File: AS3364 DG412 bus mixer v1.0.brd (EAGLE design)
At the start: 88.9 x 49.2 mm, 118 parts, among them IC1 PCA9539PW, IC10 DG412-J, IC11 DG412-J, IC14 TL074JT, IC2 TL074JT, IC3 TL072JT, IC4 TL074JT, IC6 TL072JT, IC8 DG412-J, IC9 DG412-J

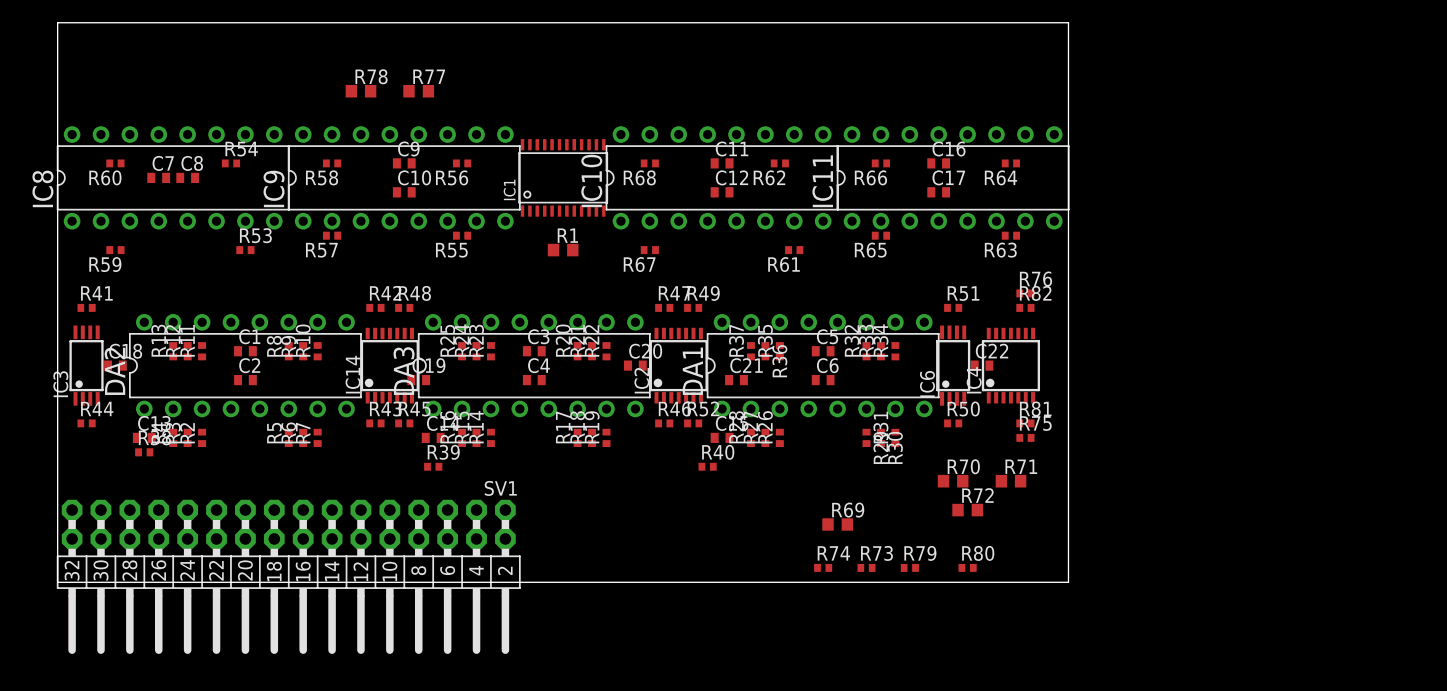
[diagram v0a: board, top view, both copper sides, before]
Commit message: Finished tracing switches and vcas internally
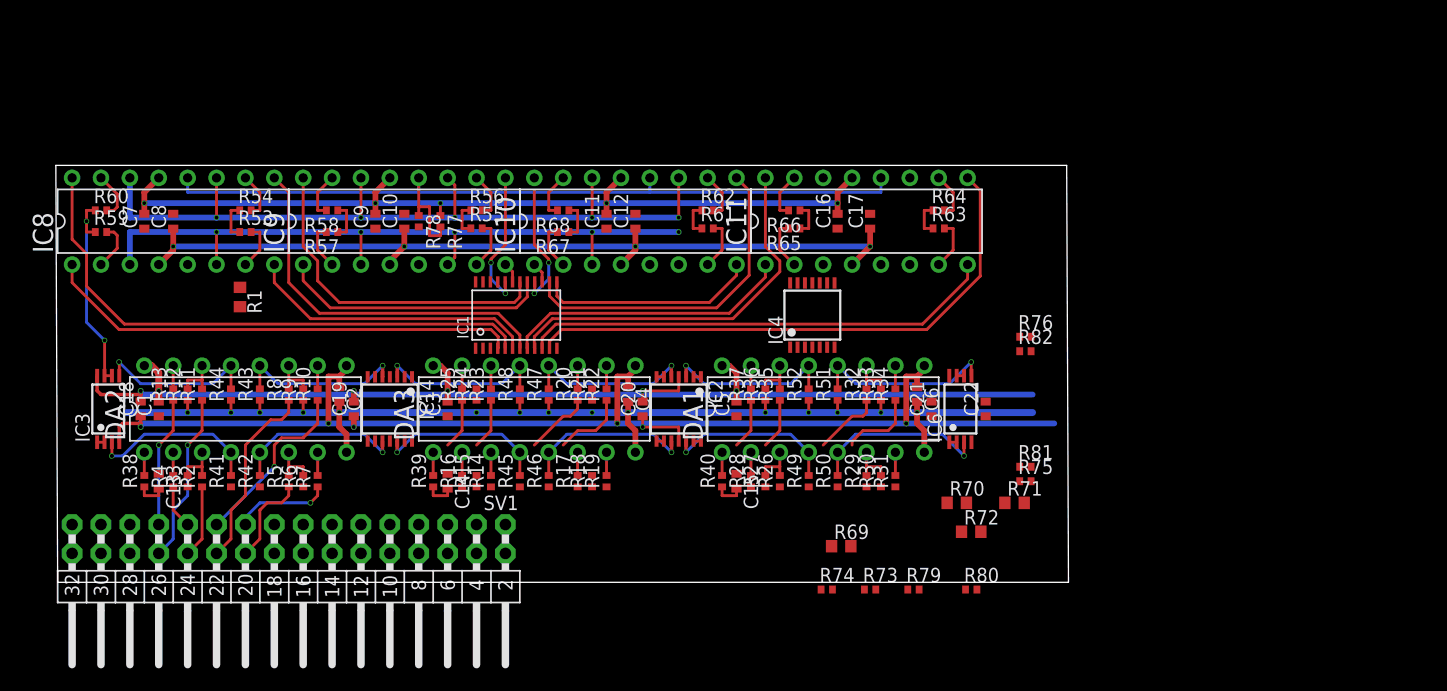
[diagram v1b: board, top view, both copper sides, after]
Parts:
- R77, R78: device rcl:R0603 -> rcl:R0402
- moved R1 28.7 mm to (16.0, 25.1), turned to 270 degrees
- moved R41 19.8 mm to (15.2, 8.89), turned to 90 degrees
- moved R49 18.3 mm to (66.0, 8.89), turned to 90 degrees
- moved R42 18.3 mm to (17.8, 8.89), turned to 90 degrees
- moved IC4 18.0 mm to (66.4, 23.5)
- moved C21 17.3 mm to (76.8, 15.2), turned to 90 degrees
- moved R44 13.0 mm to (15.2, 16.5), turned to 90 degrees
- moved IC1 12.8 mm to (40.3, 23.5)
- moved R47 12.7 mm to (43.2, 16.5), turned to 90 degrees
- moved R48 12.7 mm to (40.6, 16.5), turned to 90 degrees
- moved R51 12.7 mm to (68.6, 16.5), turned to 90 degrees
- moved R78 12.5 mm to (31.8, 31.8), turned to 270 degrees
- moved R77 11.6 mm to (33.7, 31.8), turned to 270 degrees
- moved C11 11.4 mm to (48.3, 31.8), turned to 90 degrees
- moved R46 11.4 mm to (43.2, 8.89), turned to 90 degrees
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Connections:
- net CON1: now also IC3.5; no longer IC3.3
- net CON2: now also IC3.3; no longer IC3.5
- net CON3: now also IC14.5; no longer IC14.3
- net CON4: now also IC14.10; no longer IC14.12
- net CON5: now also IC14.3; no longer IC14.5
- net CON6: now also IC14.12; no longer IC14.10
- net CON7: now also IC2.5; no longer IC2.3
- net CON8: now also IC2.10; no longer IC2.12
- net CON_O1: now also IC2.3; no longer IC2.5
- net CON_O2: now also IC2.12; no longer IC2.10
- net CON_O3: now also IC6.5; no longer IC6.3
- net CON_O4: now also IC6.3; no longer IC6.5
- net DIG_3_BUS_A: now also IC1.17; no longer IC1.8
- net DIG_3_BUS_B: now also IC1.18; no longer IC1.9
- net DIG_4_BUS_A: now also IC1.19; no longer IC1.10
- net DIG_4_BUS_B: now also IC1.20; no longer IC1.11
- net DIG_5_BUS_A: now also IC1.15; no longer IC1.13
- net DIG_5_BUS_B: now also IC1.16; no longer IC1.14
- net DIG_6_BUS_A: now also IC1.13; no longer IC1.15
- net DIG_6_BUS_B: now also IC1.14; no longer IC1.16
- net DIG_7_BUS_A: now also IC1.8; no longer IC1.17
- net DIG_7_BUS_B: now also IC1.9; no longer IC1.18
- net DIG_8_BUS_A: now also IC1.10; no longer IC1.19
- net DIG_8_BUS_B: now also IC1.11; no longer IC1.20
- net OUT1: now also IC3.6, IC3.7; no longer IC3.1, IC3.2
- net OUT2: now also IC3.1, IC3.2; no longer IC3.6, IC3.7
- net OUT3: now also IC14.6, IC14.7; no longer IC14.1, IC14.2
- net OUT4: now also IC14.8, IC14.9; no longer IC14.13, IC14.14
- net OUT5: now also IC14.1, IC14.2; no longer IC14.6, IC14.7
- net OUT6: now also IC14.13, IC14.14; no longer IC14.8, IC14.9
- net OUT7: now also IC2.6, IC2.7; no longer IC2.1, IC2.2
- net OUT8: now also IC2.8, IC2.9; no longer IC2.13, IC2.14
- net OUT_A: now also IC2.1, IC2.2; no longer IC2.6, IC2.7
- net OUT_B: now also IC2.13, IC2.14; no longer IC2.8, IC2.9
- net OUT_FX_A: now also IC6.6, IC6.7; no longer IC6.1, IC6.2
- net OUT_FX_B: now also IC6.1, IC6.2; no longer IC6.6, IC6.7
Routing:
- net -12V: track 0.00 -> 189.7 mm, vias 0 -> 10
- net +12V: track 0.00 -> 181.8 mm, vias 0 -> 11
- net GND: track 0.00 -> 104.7 mm, vias 0 -> 15
- net N$4: track 0.00 -> 74.6 mm
- net BUS_B: track 0.00 -> 69.5 mm, vias 0 -> 5
- net BUS_A: track 0.00 -> 62.8 mm, vias 0 -> 5
- net DIG_8_BUS_B: track 0.00 -> 50.0 mm
- net DIG_1_BUS_B: track 0.00 -> 49.7 mm
- net DIG_1_BUS_A: track 0.00 -> 42.1 mm
- net DIG_8_BUS_A: track 0.00 -> 41.7 mm
- net DIG_7_BUS_B: track 0.00 -> 33.8 mm
- net DIG_2_BUS_B: track 0.00 -> 33.1 mm
- net DIG_3_BUS_B: track 0.00 -> 29.7 mm
- net DIG_6_BUS_B: track 0.00 -> 29.4 mm
- net DIG_2_BUS_A: track 0.00 -> 25.5 mm
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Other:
- board size 88.9 x 49.2 mm -> 89 x 36.7 mm

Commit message: Digital lines traced
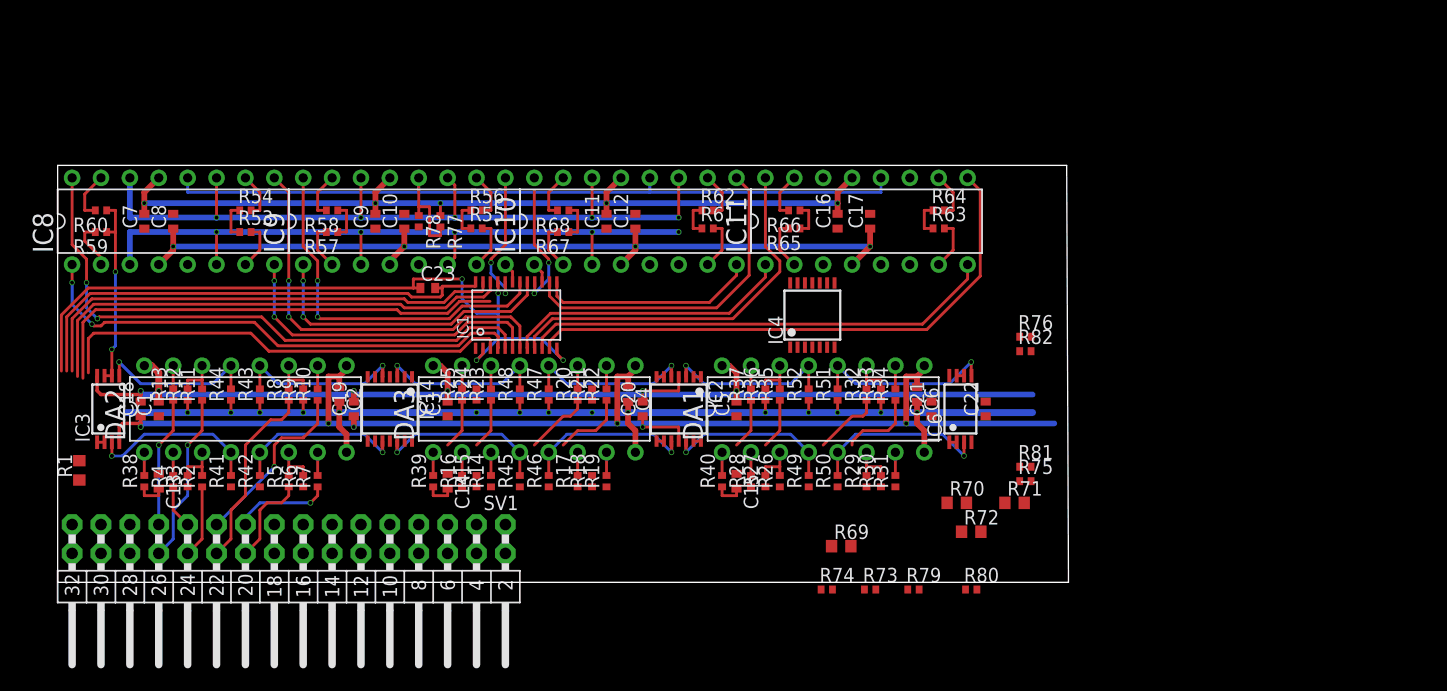
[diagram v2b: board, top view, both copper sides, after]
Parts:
- added C23: 100nF, rcl:C0402
- moved R1 20.8 mm to (1.91, 9.84), turned to 90 degrees
- turned R59 to 180 degrees
- turned R60 to 180 degrees
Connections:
- net +3V3: now also C23.2
- net DGND: now also C23.1
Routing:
- net DGND: track 0.00 -> 106.5 mm, vias 0 -> 4
- net +3V3: track 0.00 -> 43.5 mm
- net SCL: track 0.00 -> 43.3 mm
- net SDA: track 0.00 -> 42.8 mm
- net N$81: track 0.00 -> 40.5 mm
- net DIG_2_BUS_A: track 25.5 -> 28.7 mm, vias 0 -> 2
- net DIG_2_BUS_B: track 33.1 -> 36.3 mm, vias 0 -> 2
- net DIG_3_BUS_A: track 23.8 -> 26.8 mm, vias 0 -> 2
- net DIG_3_BUS_B: track 29.7 -> 32.5 mm, vias 0 -> 2
- net DIG_1_BUS_A: track 42.1 -> 44.4 mm, vias 0 -> 2
- net DIG_1_BUS_B: track 49.7 -> 52.0 mm, vias 0 -> 2
- net OUT1: track 18.3 -> 16.9 mm
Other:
- board size 89 x 36.7 mm -> 88.9 x 36.7 mm

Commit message: Moved dry/wet bus mixer to center to shorten vca-switch distances
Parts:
- moved DA1 25.4 mm to (41.9, 15.2)
- moved DA3 25.4 mm to (67.3, 15.2)
- moved R17 25.4 mm to (71.1, 8.89)
- moved R20 25.4 mm to (71.1, 16.5)
- moved R29 25.4 mm to (45.7, 8.89)
- moved R32 25.4 mm to (45.7, 16.5)
- moved R45 25.4 mm to (66.0, 8.89)
- moved R48 25.4 mm to (66.0, 16.5)
- moved R49 25.4 mm to (40.6, 8.89)
- moved R52 25.4 mm to (40.6, 16.5)
- moved C14 25.4 mm to (59.7, 8.89)
- moved C15 25.4 mm to (34.3, 8.89)
- moved C3 25.4 mm to (59.7, 15.2)
- moved C4 25.4 mm to (75.6, 16.5)
- moved C5 25.4 mm to (34.3, 15.2)
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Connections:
- net CON5: now also IC2.3; no longer IC14.3
- net CON6: now also IC2.12; no longer IC14.12
- net CON7: now also IC6.5; no longer IC2.5
- net CON8: now also IC6.3; no longer IC2.10
- net CON_O1: now also IC14.3; no longer IC2.3
- net CON_O2: now also IC14.12; no longer IC2.12
- net CON_O3: now also IC2.5; no longer IC6.5
- net CON_O4: now also IC2.10; no longer IC6.3
- net OUT5: now also IC2.1, IC2.2; no longer IC14.1, IC14.2
- net OUT6: now also IC2.13, IC2.14; no longer IC14.13, IC14.14
- net OUT7: now also IC6.6, IC6.7; no longer IC2.6, IC2.7
- net OUT8: now also IC6.1, IC6.2; no longer IC2.8, IC2.9
- net OUT_A: now also IC14.1, IC14.2; no longer IC2.1, IC2.2
- net OUT_B: now also IC14.13, IC14.14; no longer IC2.13, IC2.14
- net OUT_FX_A: now also IC2.6, IC2.7; no longer IC6.6, IC6.7
- net OUT_FX_B: now also IC2.8, IC2.9; no longer IC6.1, IC6.2
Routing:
- net OUT2: track 4.10 -> 32.6 mm, vias 0 -> 4
- net -12V: track 189.7 -> 216.8 mm
- net OUT4: track 3.13 -> 27.4 mm, vias 0 -> 2
- net OUT5: track 3.44 -> 26.7 mm, vias 0 -> 2
- net OUT7: track 3.78 -> 25.5 mm, vias 0 -> 2
- net OUT8: track 3.78 -> 24.8 mm, vias 0 -> 4
- net OUT6: track 3.13 -> 22.6 mm, vias 0 -> 2
- net BUS_FX_B: track 0.00 -> 14.6 mm, vias 0 -> 2
- net OUT3: track 3.45 -> 17.6 mm, vias 0 -> 2
- net BUS_FX_A: track 0.00 -> 13.3 mm, vias 0 -> 2
- net GND: track 104.7 -> 112.6 mm
- net +12V: track 181.8 -> 177.3 mm, vias 11 -> 12
- net BUS_A: track 62.8 -> 65.7 mm
- net CON7: track 15.1 -> 16.4 mm
- net CON_O3: track 16.4 -> 15.1 mm
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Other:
- board size 88.9 x 36.7 mm -> 120.2 x 36.7 mm

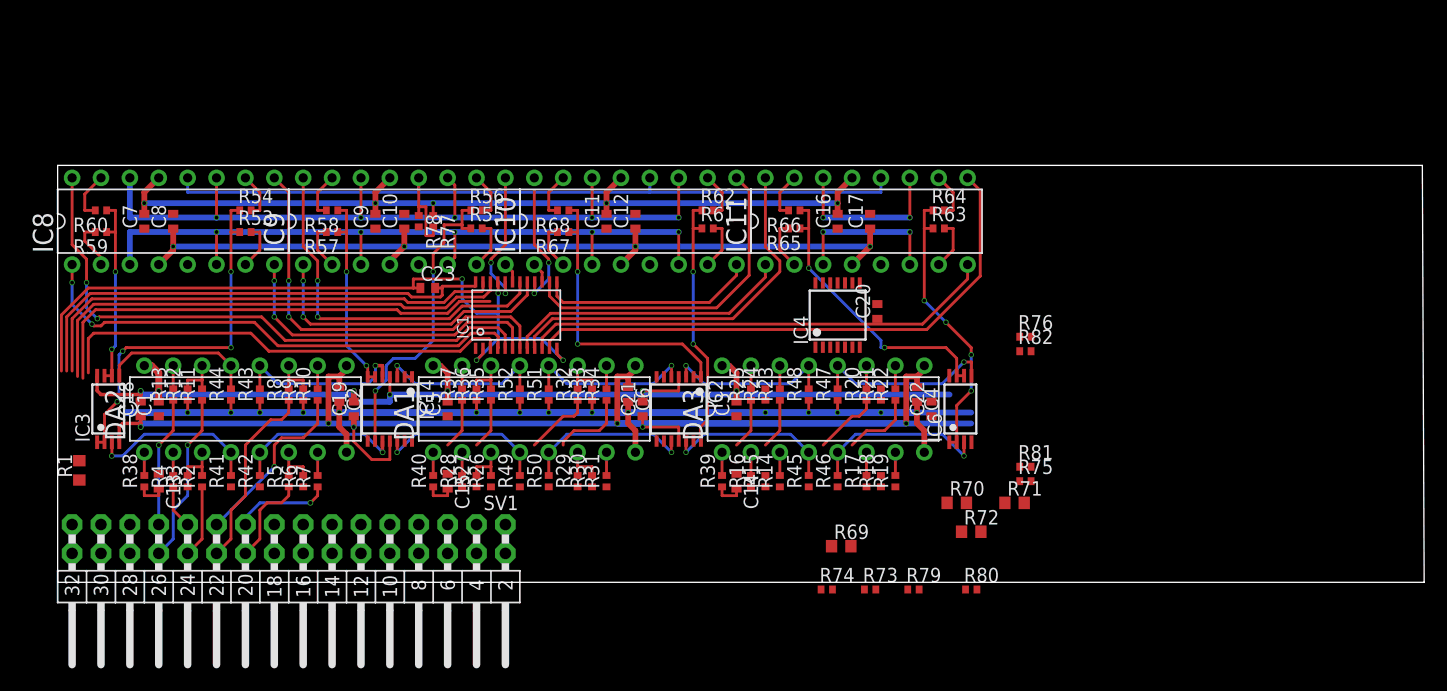
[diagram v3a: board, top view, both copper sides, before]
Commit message: Almost all signals routed except outputs
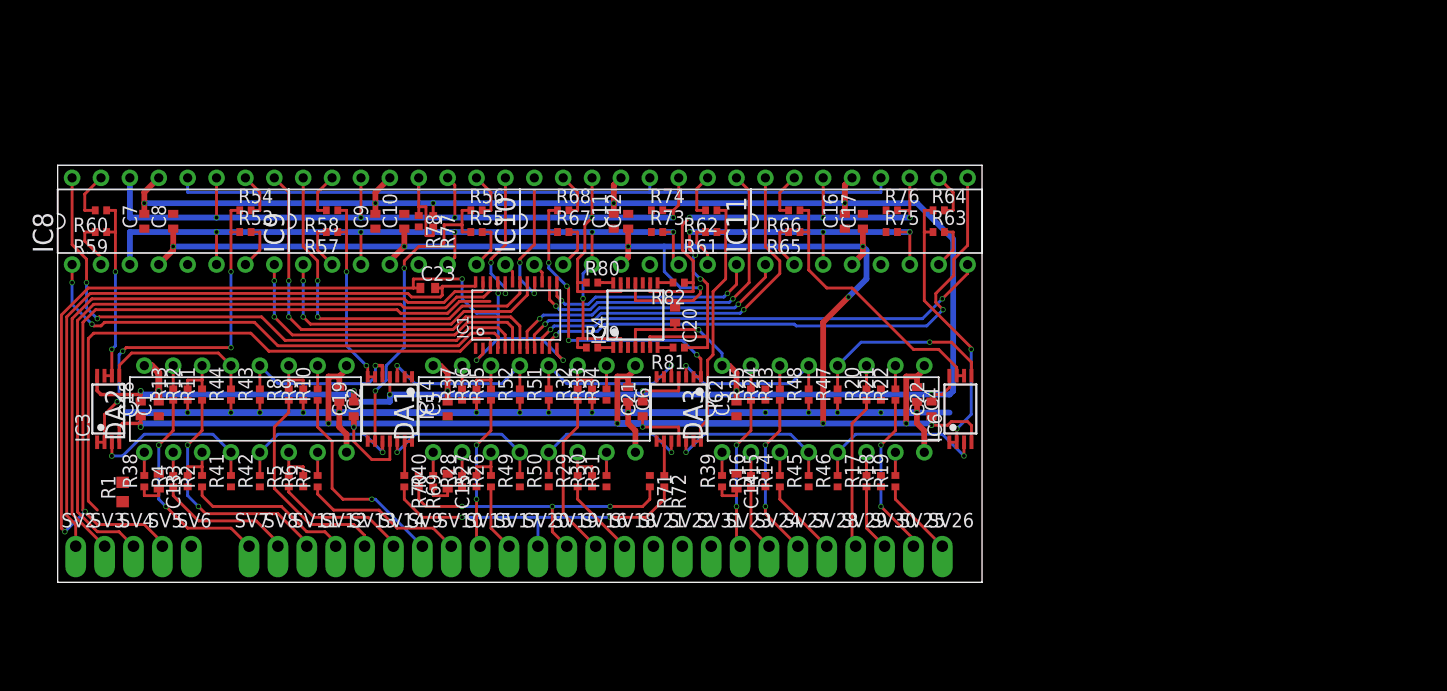
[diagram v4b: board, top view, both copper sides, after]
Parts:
- removed SV1: (no value), joakim:MA16-2WJ
- added SV10, SV11, SV12, SV13, SV14, SV15, SV16, SV17, SV18, SV19, SV2, SV20, SV21, SV22, SV23, SV24, SV25, SV26, SV27, SV28, SV29, SV3, SV30, SV31, SV4, SV5, SV6, SV7, SV8, SV9: (no value), joakim:SIP-PIN01-1J
- R69, R70, R71, R72: device rcl:R0603 -> rcl:R0402
- moved R70 48.6 mm to (30.5, 8.89), turned to 270 degrees
- moved R80 42.9 mm to (47.0, 26.4)
- moved R69 37.6 mm to (31.8, 8.89), turned to 270 degrees
- moved R73 36.6 mm to (52.7, 30.8)
- moved R74 36.5 mm to (52.7, 32.7)
- moved R79 35.4 mm to (47.0, 20.6)
- moved R81 32.2 mm to (54.6, 20.6), turned to 180 degrees
- moved R71 32.1 mm to (52.1, 8.89), turned to 270 degrees
- moved R82 31.1 mm to (54.6, 26.4), turned to 180 degrees
- moved R72 27.4 mm to (53.3, 8.89), turned to 270 degrees
- moved R75 24.9 mm to (73.3, 30.8)
- moved C20 17.8 mm to (54.3, 23.5), turned to 270 degrees
- moved IC4 17.8 mm to (50.8, 23.5)
- moved R76 16.2 mm to (73.3, 32.7)
- moved R1 4.26 mm to (5.71, 7.94)
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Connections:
- new net RST: SV6.1
- net +12V: now also SV21.1; no longer SV1.18
- net +3V3: now also SV2.1; no longer SV1.31
- net -12V: now also SV31.1; no longer SV1.15
- net CV1: now also SV11.1; no longer SV1.26
- net CV2: now also SV12.1; no longer SV1.24
- net CV3: now also SV13.1; no longer SV1.22
- net CV4: now also SV14.1; no longer SV1.20
- net CV5: now also SV27.1; no longer SV1.12
- net CV6: now also SV28.1; no longer SV1.10
- net CV7: now also SV29.1; no longer SV1.8
- net CV8: now also SV30.1; no longer SV1.6
- net CV_A_DRY: now also SV15.1
- net CV_A_WET: now also SV16.1
- net CV_B_DRY: now also SV17.1
- net CV_B_WET: now also SV18.1
- net DGND: now also SV5.1; no longer SV1.29
- net GND: now also SV22.1; no longer SV1.17
- net IN1: now also SV7.1; no longer SV1.25
- net IN2: now also SV8.1; no longer SV1.23
- net IN3: now also SV9.1; no longer SV1.21
- net IN4: now also SV10.1; no longer SV1.19
- net IN5: now also SV23.1; no longer SV1.11
- net IN6: now also SV24.1; no longer SV1.9
- net IN7: now also SV25.1; no longer SV1.7
- net IN8: now also SV26.1; no longer SV1.5
- net LPF_IN_100K_MIX: now also SV20.1
- net SCL: now also SV4.1; no longer SV1.32
- net SDA: now also SV3.1; no longer SV1.30
- net SVF_IN_100K_MIX: now also SV19.1
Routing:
- net +12V: track 177.3 -> 217.3 mm, vias 12 -> 14
- net DGND: track 106.5 -> 143.4 mm, vias 4 -> 6
- net BUS_FX_A: track 13.3 -> 45.3 mm, vias 2 -> 5
- net LPF_IN_100K_MIX: track 0.00 -> 28.9 mm, vias 0 -> 2
- net SVF_IN_100K_MIX: track 0.00 -> 27.0 mm, vias 0 -> 3
- net -12V: track 216.8 -> 242.8 mm, vias 10 -> 14
- net BUS_FX_B: track 14.6 -> 40.0 mm, vias 2 -> 3
- net SCL: track 43.3 -> 61.4 mm
- net SDA: track 42.8 -> 59.4 mm
- net +3V3: track 43.5 -> 59.3 mm
- net BUS_A: track 65.7 -> 79.3 mm, vias 5 -> 6
- net BUS_B: track 69.5 -> 82.5 mm
- net N$81: track 40.5 -> 52.9 mm
- net CV5: track 4.47 -> 14.5 mm, vias 0 -> 2
- net IN5: track 4.47 -> 13.5 mm, vias 0 -> 2
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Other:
- board size 120.2 x 36.7 mm -> 81.3 x 36.7 mm
